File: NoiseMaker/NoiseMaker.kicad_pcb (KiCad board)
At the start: 2 copper layers, 60.6 x 73.2 mm, 20 parts, among them J1 IDE_OUT, J2 IDE_IN, J3 PWR, J4 SPK, M1 Mounting, M2 Mounting, M3 Mounting, SW1 TEST, SW2 VOL_UP, SW3 VOL_DOWN

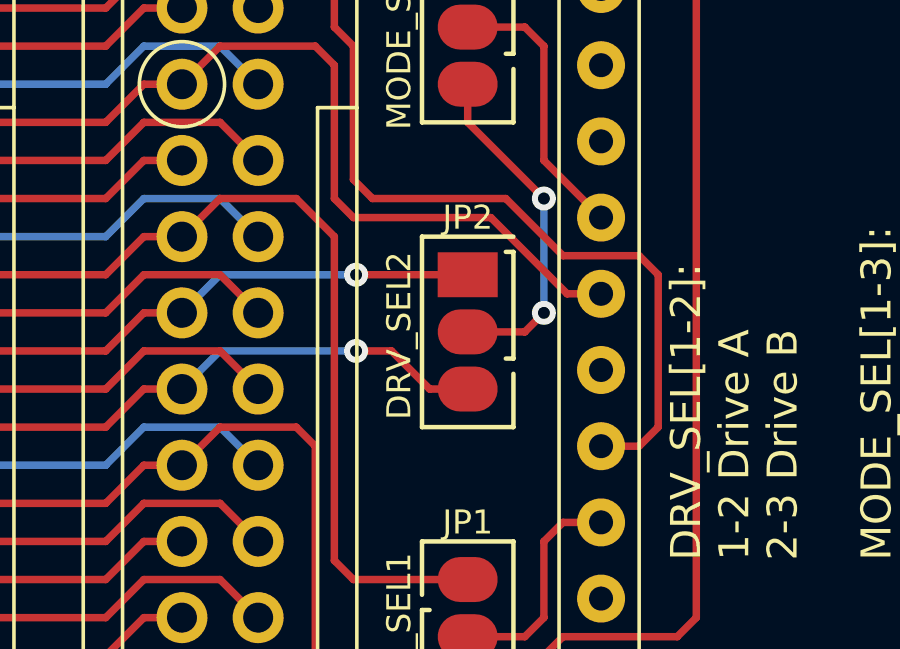
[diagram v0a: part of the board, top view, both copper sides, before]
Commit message: JP2 now THT jumper
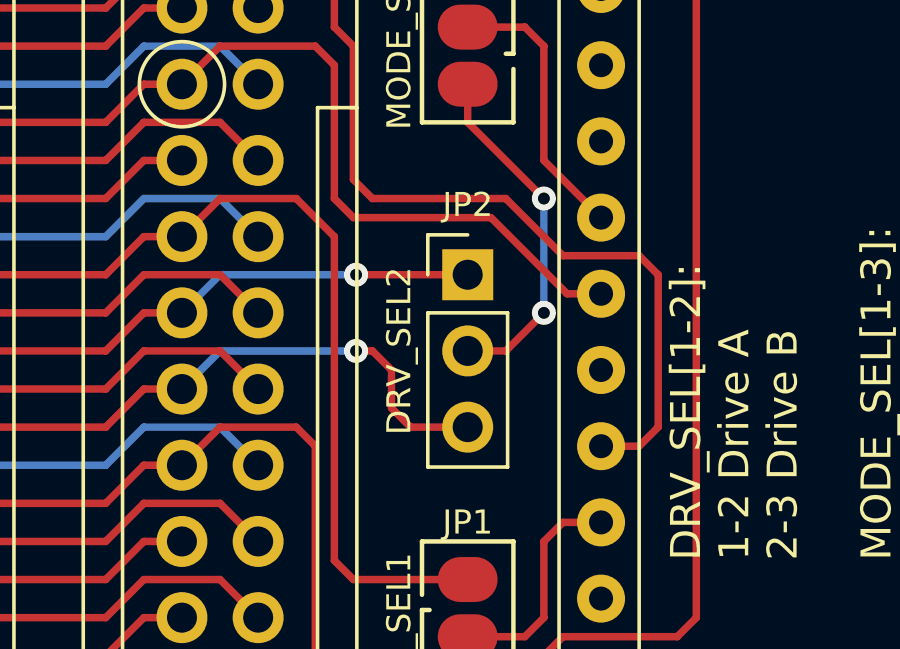
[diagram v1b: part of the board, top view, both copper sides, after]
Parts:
- JP2: footprint solder_bridge:select2 -> Connector_PinHeader_2.54mm:PinHeader_1x03_P2.54mm_Vertical
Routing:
- net /P12: track 23.1 -> 24.3 mm

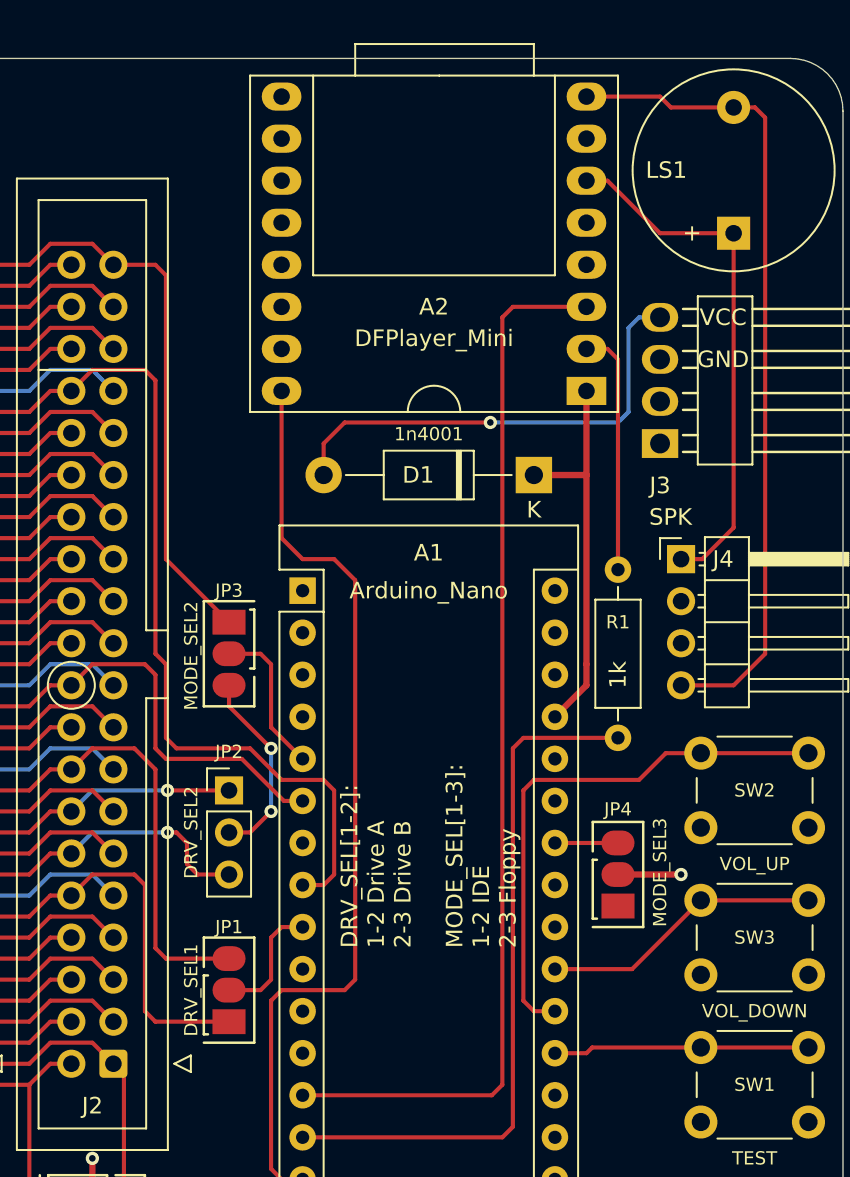
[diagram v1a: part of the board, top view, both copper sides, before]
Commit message: Account for two common passive buzzers
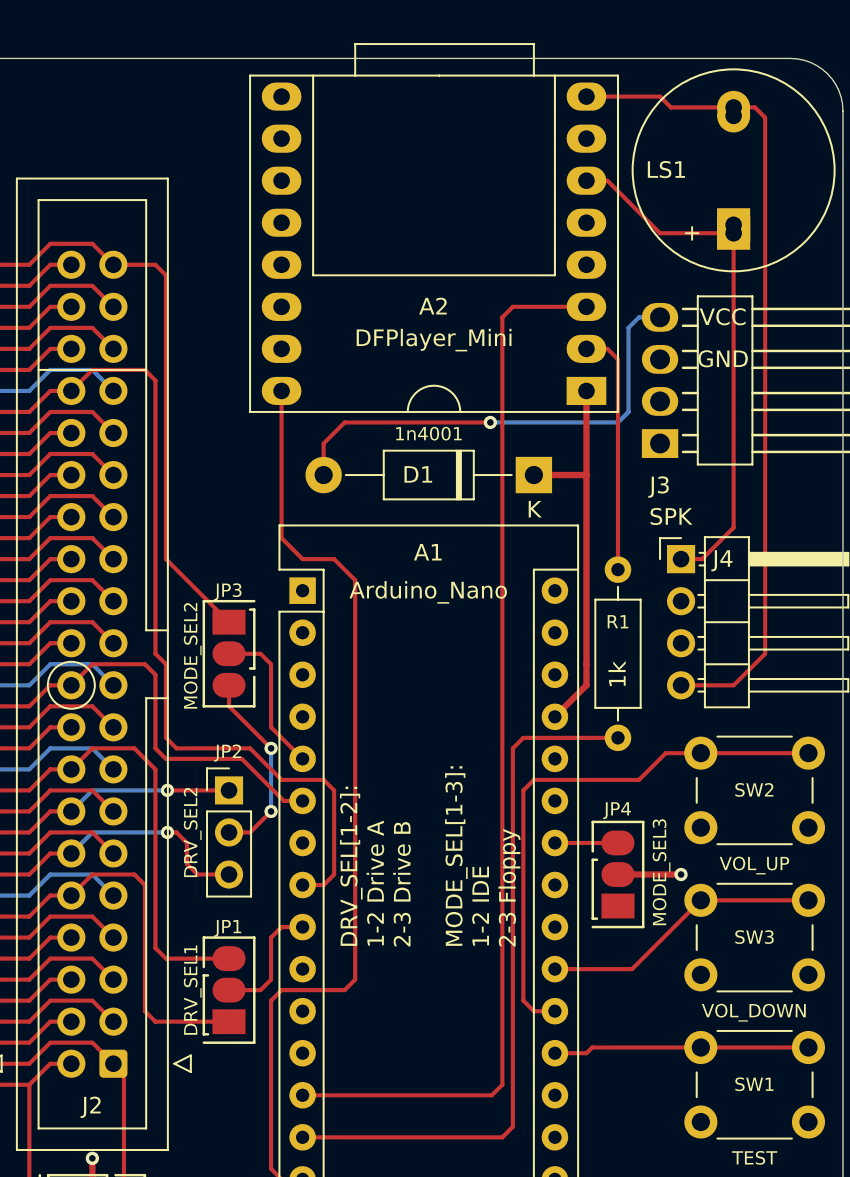
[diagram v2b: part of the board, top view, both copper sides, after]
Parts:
- LS1: footprint Buzzer_Beeper:Buzzer_12x9.5RM7.6 -> Buzzer:Buzzer_12x9.5RM7.6

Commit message: Did it properly
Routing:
- net Net-(A2-Pad8): track 49.6 -> 53.4 mm
- net Net-(A2-Pad6): track 31.9 -> 35.5 mm
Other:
- net class Audio added: clearance 0.2, trace_width 0.381, via_dia 0.8, via_drill 0.4

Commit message: Rename library
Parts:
- LS1: footprint Buzzer:Buzzer_12x9.5RM7.6 -> small_buzzer:Buzzer_12x9.5RM7.6

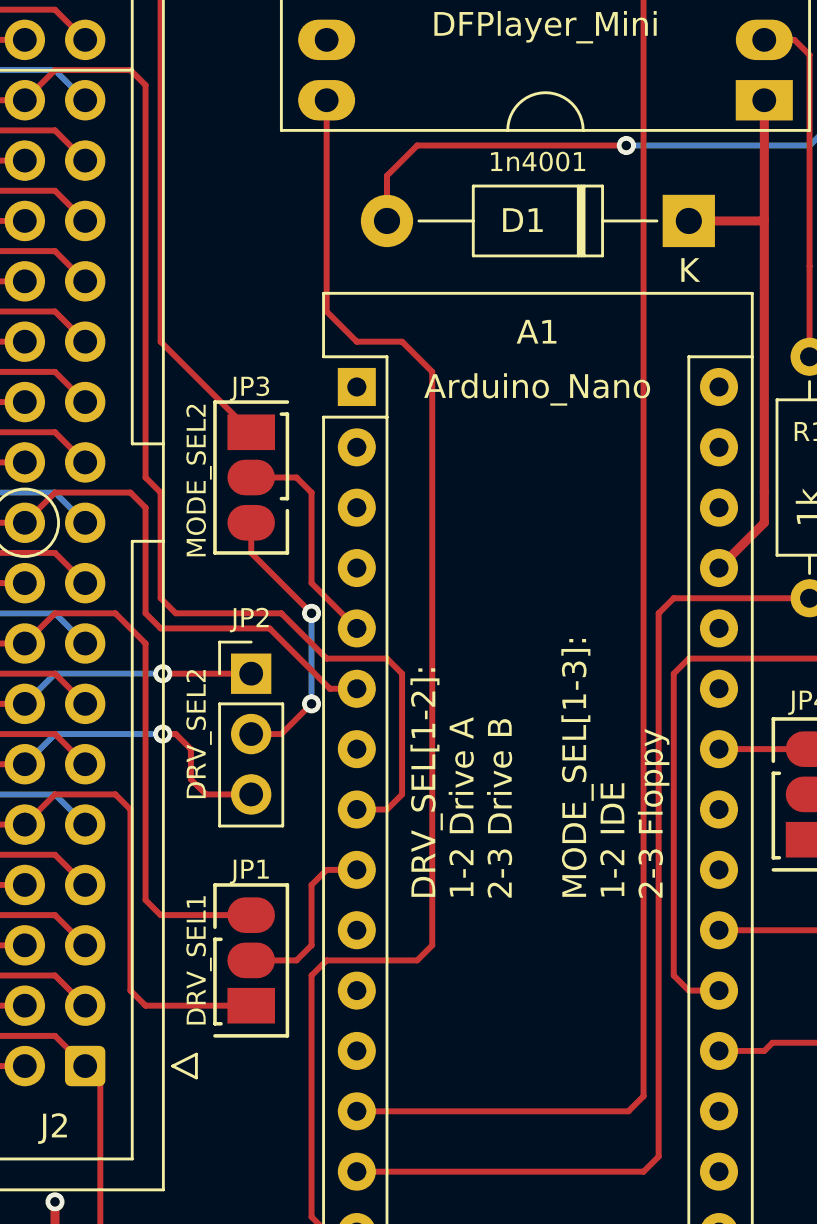
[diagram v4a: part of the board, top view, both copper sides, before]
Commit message: Update README and tweak silkscreen
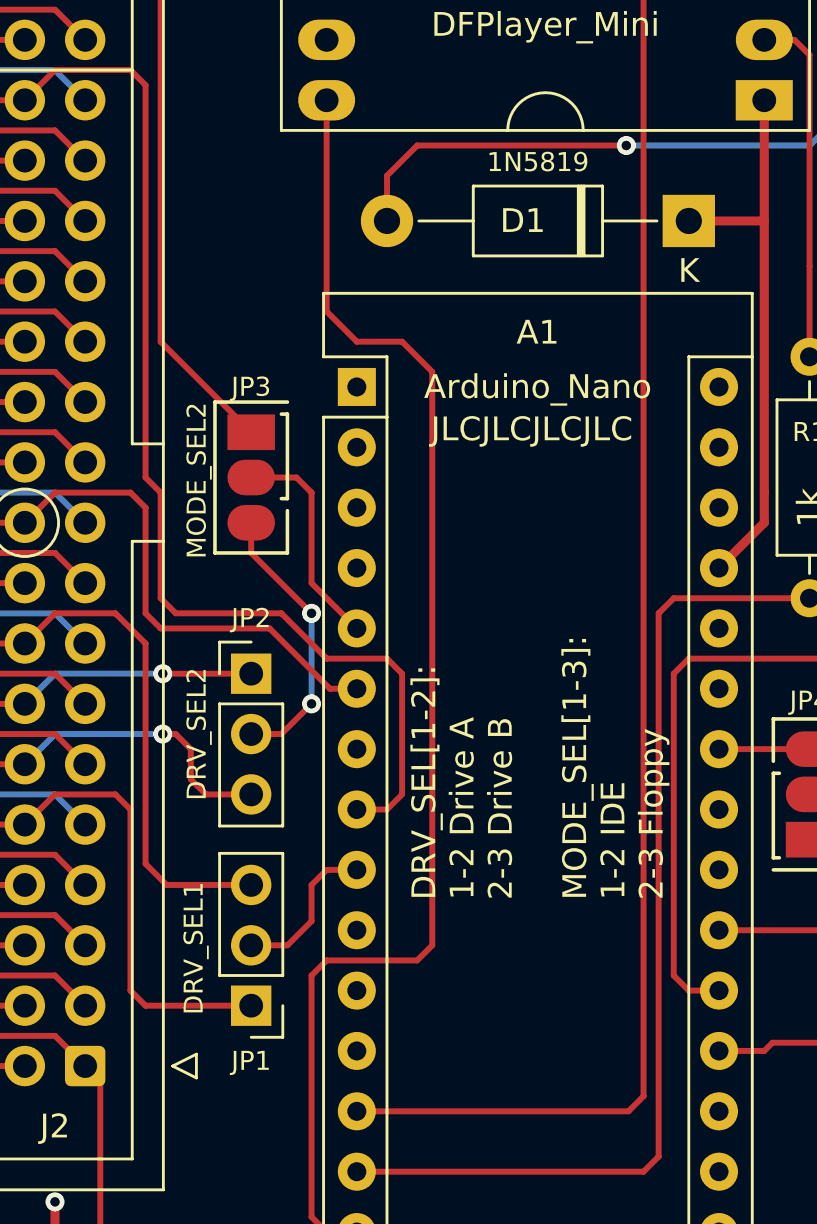
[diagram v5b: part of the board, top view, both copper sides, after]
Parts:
- D1: value 1n4001 -> 1N5819
- JP1: footprint solder_bridge:select2 -> Connector_PinHeader_2.54mm:PinHeader_1x03_P2.54mm_Vertical
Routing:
- net /P16: track 34.1 -> 32.7 mm
- net FLP_MOTOR: track 7.51 -> 6.65 mm
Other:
- board text added: "JLCJLCJLCJLC"
- board text added: "NoiseMaker IDE/Floppy (rev. B) github.com/tebl"
- board text removed: "NoiseMaker IDE/Floppy github.com/tebl"
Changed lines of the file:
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@@
   (general
     (thickness 1.6)
-    (drawings 14)
+    (drawings 15)
     (tracks 312)
     (zones 0)
@@
       (effects (font (size 1 1) (thickness 0.15)))
     )
-    (fp_text value 1n4001 (at 6.35 2.47) (layer F.SilkS)
+    (fp_text value 1N5819 (at 6.35 2.47) (layer F.SilkS)
       (effects (font (size 0.8 0.8) (thickness 0.1)))
     )
@@
   )
   (module solder_bridge:select2 (layer F.Cu)
-    (at 148.648 126.365 180)
-    (descr "Through hole straight pin header, 1x02, 1.00mm pitch, single row")
-    (tags "Through hole pin header THT 1x02 1.00mm single row")
-    (fp_text reference JP1 (at 0 5.715) (layer F.SilkS)
-      (effects (font (size 0.8 0.8) (thickness 0.1)))
-    )
-    (fp_text value DRV_SEL1 (at 2.286 1.905 90) (layer F.SilkS)
-      (effects (font (size 0.8 0.8) (thickness 0.1)))
-    )
-    (fp_line (start 1.27 -0.762) (end 1.524 -0.762) (layer F.SilkS) (width 0.15))
-    (fp_line (start -1.524 5.08) (end -1.524 -1.27) (layer F.SilkS) (width 0.15))
-    (fp_line (start 1.524 -1.27) (end -1.524 -1.27) (layer F.SilkS) (width 0.15))
-    (fp_line (start 1.27 2.794) (end 1.524 2.794) (layer F.SilkS) (width 0.15))
-    (fp_line (start 1.524 2.794) (end 1.524 -0.762) (layer F.SilkS) (width 0.15))
-    (fp_line (start 1.524 3.302) (end 1.524 5.08) (layer F.SilkS) (width 0.15))
-    (fp_line (start -1.524 5.08) (end 1.524 5.08) (layer F.SilkS) (width 0.15))
-    (fp_text user %R (at 0 5.842 180) (layer F.Fab)
-      (effects (font (size 0.8 0.8) (thickness 0.1)))
-    )
-    (pad 3 smd oval (at 0 3.81 180) (size 2 1.5) (layers F.Cu F.Paste F.Mask)
-      (net 24 /P16))
-    (pad 2 smd oval (at 0 1.905 180) (size 2 1.5) (layers F.Cu F.Paste F.Mask)
-      (net 47 FLP_MOTOR))
-    (pad 1 smd rect (at 0 0 180) (size 2 1.5) (layers F.Cu F.Paste F.Mask)
-      (net 18 /P10))
-    (model ${KISYS3DMOD}/Pin_Headers.3dshapes/Pin_Header_Straight_1x02_Pitch1.00mm.wrl
-      (at (xyz 0 0 0))
-      (scale (xyz 1 1 1))
-      (rotate (xyz 0 0 0))
-    )
-  )
-  (module solder_bridge:select2 (layer F.Cu)
     (at 148.648 102.235)
     (descr "Through hole straight pin header, 1x02, 1.00mm pitch, single row")
@@
     )
   )
+  (module Connector_PinHeader_2.54mm:PinHeader_1x03_P2.54mm_Vertical (layer F.Cu)
+    (at 148.648 126.365 180)
+    (descr "Through hole straight pin header, 1x03, 2.54mm pitch, single row")
+    (tags "Through hole pin header THT 1x03 2.54mm single row")
+    (fp_text reference JP1 (at 0 -2.33) (layer F.SilkS)
+      (effects (font (size 0.8 0.8) (thickness 0.1)))
+    )
+    (fp_text value DRV_SEL1 (at 2.413 2.413 90) (layer F.SilkS)
+      (effects (font (size 0.8 0.8) (thickness 0.1)))
+    )
+    (fp_line (start -0.635 -1.27) (end 1.27 -1.27) (layer F.Fab) (width 0.1))
+    (fp_line (start 1.27 -1.27) (end 1.27 6.35) (layer F.Fab) (width 0.1))
+    (fp_line (start 1.27 6.35) (end -1.27 6.35) (layer F.Fab) (width 0.1))
+    (fp_line (start -1.27 6.35) (end -1.27 -0.635) (layer F.Fab) (width 0.1))
+    (fp_line (start -1.27 -0.635) (end -0.635 -1.27) (layer F.Fab) (width 0.1))
+    (fp_line (start -1.33 6.41) (end 1.33 6.41) (layer F.SilkS) (width 0.12))
+    (fp_line (start -1.33 1.27) (end -1.33 6.41) (layer F.SilkS) (width 0.12))
+    (fp_line (start 1.33 1.27) (end 1.33 6.41) (layer F.SilkS) (width 0.12))
+    (fp_line (start -1.33 1.27) (end 1.33 1.27) (layer F.SilkS) (width 0.12))
+    (fp_line (start -1.33 0) (end -1.33 -1.33) (layer F.SilkS) (width 0.12))
+    (fp_line (start -1.33 -1.33) (end 0 -1.33) (layer F.SilkS) (width 0.12))
+    (fp_line (start -1.8 -1.8) (end -1.8 6.85) (layer F.CrtYd) (width 0.05))
+    (fp_line (start -1.8 6.85) (end 1.8 6.85) (layer F.CrtYd) (width 0.05))
+    (fp_line (start 1.8 6.85) (end 1.8 -1.8) (layer F.CrtYd) (width 0.05))
+    (fp_line (start 1.8 -1.8) (end -1.8 -1.8) (layer F.CrtYd) (width 0.05))
+    (fp_text user %R (at 0 2.54 90) (layer F.Fab)
+      (effects (font (size 1 1) (thickness 0.15)))
+    )
+    (pad 1 thru_hole rect (at 0 0 180) (size 1.7 1.7) (drill 1) (layers *.Cu *.Mask)
+      (net 18 /P10))
+    (pad 2 thru_hole oval (at 0 2.54 180) (size 1.7 1.7) (drill 1) (layers *.Cu *.Mask)
+      (net 47 FLP_MOTOR))
+    (pad 3 thru_hole oval (at 0 5.08 180) (size 1.7 1.7) (drill 1) (layers *.Cu *.Mask)
+      (net 24 /P16))
+    (model ${KISYS3DMOD}/Connector_PinHeader_2.54mm.3dshapes/PinHeader_1x03_P2.54mm_Vertical.wrl
+      (at (xyz 0 0 0))
+      (scale (xyz 1 1 1))
+      (rotate (xyz 0 0 0))
+    )
+  )
+  (gr_text JLCJLCJLCJLC (at 160.459 102.108) (layer F.SilkS)
+    (effects (font (size 1 1) (thickness 0.15)))
+  )
   (gr_text "MODE_SEL[1-3]:\n1-2 IDE\n2-3 Floppy" (at 163.888 121.92 90) (layer F.SilkS)
     (effects (font (size 1 1) (thickness 0.15)) (justify left))
@@
   (gr_line (start 128.328 141.37) (end 182.558 141.37) (layer Edge.Cuts) (width 0.05))
   (gr_line (start 182.558 68.18) (end 128.328 68.18) (layer Edge.Cuts) (width 0.05))
-  (gr_text "NoiseMaker IDE/Floppy\ngithub.com/tebl" (at 134.678 104.775 90) (layer B.SilkS)
+  (gr_text "NoiseMaker IDE/Floppy (rev. B)\ngithub.com/tebl" (at 134.678 104.775 90) (layer B.SilkS)
     (effects (font (size 1 1) (thickness 0.15)) (justify mirror))
   )
@@
   (segment (start 143.568 118.11) (end 143.568 125.73) (width 0.25) (layer F.Cu) (net 18))
   (segment (start 142.933 117.475) (end 143.568 118.11) (width 0.25) (layer F.Cu) (net 18))
-  (segment (start 144.203 126.365) (end 148.648 126.365) (width 0.25) (layer F.Cu) (net 18) (status 20))
   (segment (start 140.393 117.475) (end 142.933 117.475) (width 0.25) (layer F.Cu) (net 18))
   (segment (start 139.123 118.745) (end 140.393 117.475) (width 0.25) (layer F.Cu) (net 18) (status 10))
+  (segment (start 144.203 126.365) (end 148.648 126.365) (width 0.25) (layer F.Cu) (net 18) (status 20))
   (segment (start 140.393 114.935) (end 137.853 114.935) (width 0.25) (layer F.Cu) (net 19))
   (segment (start 141.663 116.205) (end 140.393 114.935) (width 0.25) (layer F.Cu) (net 19) (status 10))
@@
   (segment (start 142.933 109.855) (end 140.393 109.855) (width 0.25) (layer F.Cu) (net 24))
   (segment (start 144.203 111.125) (end 142.933 109.855) (width 0.25) (layer F.Cu) (net 24))
-  (segment (start 144.203 121.92) (end 144.203 111.125) (width 0.25) (layer F.Cu) (net 24))
-  (segment (start 144.838 122.555) (end 144.203 121.92) (width 0.25) (layer F.Cu) (net 24))
-  (segment (start 148.648 122.555) (end 144.838 122.555) (width 0.25) (layer F.Cu) (net 24) (status 10))
+  (segment (start 145.092 121.285) (end 144.203 120.396) (width 0.25) (layer F.Cu) (net 24))
+  (segment (start 148.648 121.285) (end 145.092 121.285) (width 0.25) (layer F.Cu) (net 24) (status 10))
+  (segment (start 144.203 120.396) (end 144.203 111.125) (width 0.25) (layer F.Cu) (net 24))
   (segment (start 140.393 107.315) (end 137.853 107.315) (width 0.25) (layer F.Cu) (net 25))
   (segment (start 141.663 108.585) (end 140.393 107.315) (width 0.25) (layer F.Cu) (net 25) (status 10))
@@
   (segment (start 166.428 109.22) (end 165.793 109.855) (width 0.25) (layer F.Cu) (net 46))
   (segment (start 172.143 109.22) (end 166.428 109.22) (width 0.25) (layer F.Cu) (net 46) (status 10))
-  (segment (start 148.648 124.46) (end 150.553 124.46) (width 0.25) (layer F.Cu) (net 47) (status 10))
-  (segment (start 150.553 124.46) (end 151.188 123.825) (width 0.25) (layer F.Cu) (net 47))
-  (segment (start 151.188 123.825) (end 151.188 121.285) (width 0.25) (layer F.Cu) (net 47))
   (segment (start 151.823 120.65) (end 153.093 120.65) (width 0.25) (layer F.Cu) (net 47) (status 20))
   (segment (start 151.188 121.285) (end 151.823 120.65) (width 0.25) (layer F.Cu) (net 47))
+  (segment (start 150.172 123.825) (end 151.188 122.809) (width 0.25) (layer F.Cu) (net 47))
+  (segment (start 148.648 123.825) (end 150.172 123.825) (width 0.25) (layer F.Cu) (net 47) (status 10))
+  (segment (start 151.188 122.809) (end 151.188 121.285) (width 0.25) (layer F.Cu) (net 47))
   (segment (start 137.853 88.265) (end 139.123 88.265) (width 0.25) (layer F.Cu) (net 48) (status 20))
   (segment (start 127.693 88.265) (end 128.963 89.535) (width 0.25) (layer F.Cu) (net 48) (status 10))
